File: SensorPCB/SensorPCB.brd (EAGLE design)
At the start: 37 x 65 mm, 31 parts, among them T1 33u

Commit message: add GND
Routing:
- net GND: track 25.0 -> 75.0 mm, vias 3 -> 6
- net SWCLK: track 31.8 -> 31.2 mm

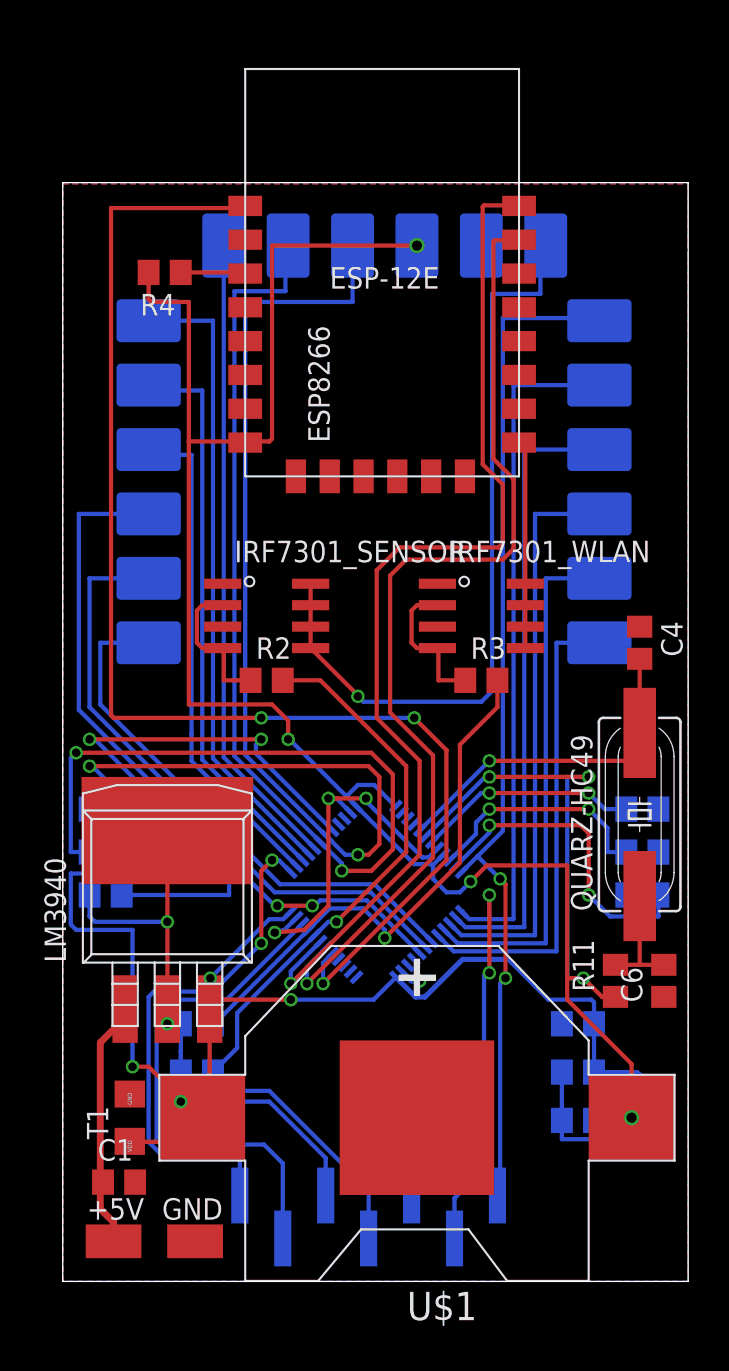
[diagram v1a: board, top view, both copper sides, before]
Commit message: edit tname and bname
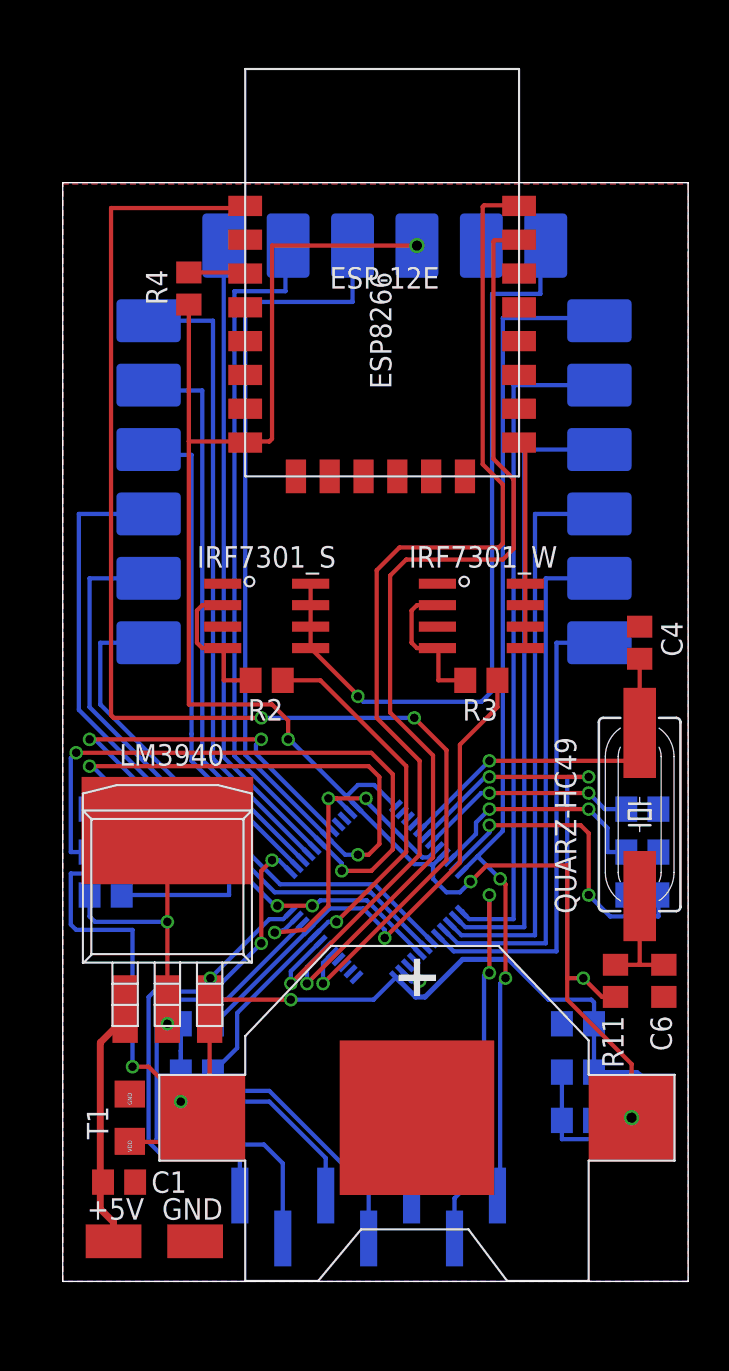
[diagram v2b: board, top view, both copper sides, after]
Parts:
- moved R4 1.72 mm to (7.46, 58.7), turned to 270 degrees
- renumbered IRF7301_SENSOR to IRF7301_S, IRF7301_WLAN to IRF7301_W
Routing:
- net +3V3: track 208.5 -> 204.3 mm

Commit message: closed #1
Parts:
- removed U$2: 5V_POWER_SUPPLY, 5V_POWER_SUPPLY:5V_POWER_SUPPLY
- added JP1: (no value), pinhead:1X02SMD
- moved C1 5.90 mm to (8.73, 3.49), turned to 270 degrees
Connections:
- net +5V: now also JP1.1; no longer U$2.MINUS
- net GND: now also JP1.2; no longer U$2.PLUS
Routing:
- net +5V: track 16.7 -> 19.3 mm
- net OSC_OUT: track 28.9 -> 27.9 mm
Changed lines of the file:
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@@
 <layers>
 <layer number="1" name="Top" color="4" fill="1" visible="yes" active="yes"/>
-<layer number="16" name="Bottom" color="1" fill="1" visible="no" active="yes"/>
+<layer number="16" name="Bottom" color="1" fill="1" visible="yes" active="yes"/>
 <layer number="17" name="Pads" color="2" fill="1" visible="yes" active="yes"/>
 <layer number="18" name="Vias" color="2" fill="1" visible="yes" active="yes"/>
@@
 <dimension x1="0" y1="0" x2="37" y2="0" x3="18.5" y3="-10" textsize="1.778" layer="1"/>
 <dimension x1="37" y1="0" x2="37" y2="65" x3="58.7375" y3="32.5" textsize="1.778" layer="1"/>
-<text x="1.42875" y="3.65125" size="1.27" layer="25">+5V</text>
-<text x="5.87375" y="3.65125" size="1.27" layer="25">GND</text>
+<text x="1.74625" y="0.79375" size="1.27" layer="25">+5V</text>
+<text x="4.445" y="5.3975" size="1.27" layer="25">GND</text>
 </plain>
 <attributes>
@@
 </autorouter>
 <elements>
-<element name="C1" library="rcl" package="C0805" value="470n" x="3.33375" y="5.87375" smashed="yes">
-<attribute name="NAME" x="5.23875" y="5.23875" size="1.27" layer="25"/>
-<attribute name="VALUE" x="2.06375" y="3.33375" size="1.27" layer="27"/>
+<element name="C1" library="rcl" package="C0805" value="470n" x="8.73125" y="3.4925" smashed="yes" rot="R270">
+<attribute name="NAME" x="8.09625" y="1.5875" size="1.27" layer="25" rot="R270"/>
+<attribute name="VALUE" x="6.19125" y="4.7625" size="1.27" layer="27" rot="R270"/>
 </element>
 <element name="C10" library="rcl" package="C0805" value="100n" x="34.29" y="27.94" smashed="yes" rot="MR180">
@@
 </element>
 <element name="U$5" library="breakout_base" package="BREAKOUT_FOOTPRINT_V1" value="BREAKOUT_FP_V1" x="33.655" y="63.1825" rot="MR270"/>
-<element name="U$2" library="5V_POWER_SUPPLY" package="5V_POWER_SUPPLY" value="5V_POWER_SUPPLY" x="5.3975" y="2.38125" rot="R180"/>
 <element name="R4" library="rcl" package="R0805" value="10k" x="7.46125" y="58.7375" smashed="yes" rot="R270">
 <attribute name="NAME" x="4.92125" y="59.84875" size="1.27" layer="25" rot="R270"/>
 <attribute name="VALUE" x="4.92125" y="59.3725" size="1.27" layer="27" rot="R270"/>
+</element>
+<element name="JP1" library="pinhead" package="1X02SMD" value="" x="5.08" y="3.65125" smashed="yes">
+<attribute name="VALUE" x="2.54" y="0.47625" size="1.27" layer="27"/>
 </element>
 </elements>
@@
 <contactref element="U$5" pad="P$17"/>
 <contactref element="U$1" pad="-"/>
-<contactref element="U$2" pad="PLUS"/>
 <polygon width="0.254" layer="1">
 <vertex x="0" y="64.92875"/>
@@
 <wire x1="6.9875" y1="15.24" x2="6.9875" y2="12.3825" width="0.254" layer="16"/>
 <wire x1="6.19125" y1="16.11" x2="6.19125" y2="15.39875" width="0.254" layer="1"/>
-<via x="6.19125" y="15.24" extent="1-16" drill="0.5"/>
-<wire x1="6.19125" y1="15.39875" x2="6.19125" y2="15.24" width="0.254" layer="1"/>
-<wire x1="6.19125" y1="15.24" x2="6.9875" y2="15.24" width="0.254" layer="16"/>
+<via x="6.35" y="15.24" extent="1-16" drill="0.5"/>
+<wire x1="6.19125" y1="15.39875" x2="6.35" y2="15.24" width="0.254" layer="1"/>
+<wire x1="6.35" y1="15.24" x2="6.9875" y2="15.24" width="0.254" layer="16"/>
 <wire x1="6.9875" y1="12.3825" x2="6.9875" y2="13.65" width="0.254" layer="16"/>
 <wire x1="6.9875" y1="13.65" x2="6.985" y2="13.6525" width="0.254" layer="16"/>
@@
 <wire x1="1.905" y1="21.2725" x2="6.19125" y2="21.2725" width="0.254" layer="16"/>
 <via x="6.19125" y="21.2725" extent="1-16" drill="0.5"/>
+<contactref element="JP1" pad="2"/>
 </signal>
 <signal name="+3V3">
@@
 <wire x1="7.62" y1="9.525" x2="6.9875" y2="9.525" width="0.254" layer="1"/>
 <wire x1="6.9875" y1="9.525" x2="6.985" y2="9.5275" width="0.254" layer="1"/>
-<wire x1="6.985" y1="9.5275" x2="6.985" y2="10.63625" width="0.254" layer="1"/>
+<wire x1="6.985" y1="9.5275" x2="6.985" y2="10.4775" width="0.254" layer="1"/>
 <wire x1="8.255" y1="9.68375" x2="8.69125" y2="10.12" width="0.254" layer="1"/>
 <wire x1="8.69125" y1="10.12" x2="8.69125" y2="16.11" width="0.254" layer="1"/>
@@
 <wire x1="4.1275" y1="12.7" x2="5.08" y2="12.7" width="0.254" layer="1"/>
 <wire x1="6.9875" y1="9.525" x2="6.985" y2="9.5275" width="0.254" layer="16"/>
-<wire x1="6.985" y1="9.5275" x2="6.985" y2="10.63625" width="0.254" layer="16"/>
-<via x="6.985" y="10.63625" extent="1-16" drill="0.5"/>
+<wire x1="6.985" y1="9.5275" x2="6.985" y2="10.4775" width="0.254" layer="16"/>
+<via x="6.985" y="10.4775" extent="1-16" drill="0.5"/>
 <wire x1="12.22375" y1="10.63625" x2="15.5575" y2="7.3025" width="0.254" layer="16"/>
-<wire x1="6.985" y1="10.63625" x2="12.22375" y2="10.63625" width="0.254" layer="16"/>
 <wire x1="5.08" y1="12.7" x2="6.985" y2="10.795" width="0.254" layer="1"/>
-<wire x1="6.985" y1="10.795" x2="6.985" y2="10.63625" width="0.254" layer="1"/>
+<wire x1="6.985" y1="10.795" x2="6.985" y2="10.4775" width="0.254" layer="1"/>
 <wire x1="7.46125" y1="57.7875" x2="7.46125" y2="49.68875" width="0.254" layer="1"/>
+<wire x1="6.985" y1="10.4775" x2="7.14375" y2="10.63625" width="0.254" layer="16"/>
+<wire x1="7.14375" y1="10.63625" x2="12.22375" y2="10.63625" width="0.254" layer="16"/>
 </signal>
 <signal name="+5V">
 <contactref element="LM3940" pad="1"/>
 <contactref element="C1" pad="1"/>
-<contactref element="U$2" pad="MINUS"/>
-<wire x1="3.0055" y1="3.18575" x2="3.0055" y2="2.37625" width="0.4064" layer="1"/>
-<wire x1="2.38375" y1="5.87375" x2="2.2225" y2="6.18875" width="0.4064" layer="1"/>
-<wire x1="2.2225" y1="6.18875" x2="2.2225" y2="4.28625" width="0.4064" layer="1"/>
-<wire x1="2.2225" y1="4.28625" x2="3.0055" y2="3.50325" width="0.4064" layer="1"/>
-<wire x1="3.0055" y1="3.50325" x2="3.0055" y2="2.37625" width="0.4064" layer="1"/>
-<wire x1="2.38375" y1="5.87375" x2="2.2225" y2="6.19375" width="0.4064" layer="1"/>
-<wire x1="2.2225" y1="6.19375" x2="2.2225" y2="14.12875" width="0.4064" layer="1"/>
+<wire x1="2.2225" y1="6.50875" x2="2.2225" y2="14.12875" width="0.4064" layer="1"/>
 <wire x1="4.1675" y1="16.07375" x2="3.69125" y2="16.11" width="0.4064" layer="1"/>
 <wire x1="2.2225" y1="14.12875" x2="3.69125" y2="15.5975" width="0.4064" layer="1"/>
 <wire x1="3.69125" y1="15.5975" x2="3.69125" y2="16.11" width="0.4064" layer="1"/>
+<contactref element="JP1" pad="1"/>
+<wire x1="3.81" y1="4.92125" x2="2.2225" y2="6.50875" width="0.4064" layer="1"/>
+<wire x1="3.81" y1="4.92125" x2="3.96875" y2="5.08" width="0.4064" layer="1"/>
+<wire x1="8.73125" y1="4.4425" x2="8.73125" y2="5.23875" width="0.4064" layer="1"/>
+<wire x1="8.73125" y1="5.23875" x2="8.41375" y2="5.55625" width="0.4064" layer="1"/>
+<wire x1="8.41375" y1="5.55625" x2="5.08" y2="5.55625" width="0.4064" layer="1"/>
+<wire x1="5.08" y1="5.55625" x2="4.445" y2="4.92125" width="0.4064" layer="1"/>
+<wire x1="4.445" y1="4.92125" x2="3.81" y2="4.92125" width="0.4064" layer="1"/>
 </signal>
 <signal name="SWCLK">
@@
 <wire x1="29.845" y1="29.845" x2="29.845" y2="17.93875" width="0.254" layer="16"/>
 <wire x1="30.7975" y1="17.93875" x2="29.845" y2="17.93875" width="0.254" layer="16"/>
-<wire x1="29.845" y1="17.93875" x2="30.7975" y2="17.93875" width="0.254" layer="1"/>
+<wire x1="29.845" y1="17.93875" x2="30.7975" y2="17.93875" width="0" layer="19" extent="1-16"/>
 <wire x1="30.7975" y1="17.93875" x2="31.90875" y2="16.8275" width="0.254" layer="1"/>
 <wire x1="31.90875" y1="16.8275" x2="32.385" y2="16.8275" width="0.254" layer="1"/>

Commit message: closed #3
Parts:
- moved C1 7.35 mm to (1.59, 5.24)
- moved JP1 1.44 mm to (6.51, 3.49)
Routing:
- net GND: track 74.9 -> 88.1 mm
- net +5V: track 19.3 -> 15.5 mm
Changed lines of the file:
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@@
 <layer number="24" name="bOrigins" color="15" fill="1" visible="yes" active="yes"/>
 <layer number="25" name="tNames" color="7" fill="1" visible="yes" active="yes"/>
-<layer number="26" name="bNames" color="7" fill="1" visible="no" active="yes"/>
-<layer number="27" name="tValues" color="7" fill="1" visible="no" active="yes"/>
-<layer number="28" name="bValues" color="7" fill="1" visible="no" active="yes"/>
+<layer number="26" name="bNames" color="7" fill="1" visible="yes" active="yes"/>
+<layer number="27" name="tValues" color="7" fill="1" visible="yes" active="yes"/>
+<layer number="28" name="bValues" color="7" fill="1" visible="yes" active="yes"/>
 <layer number="29" name="tStop" color="7" fill="3" visible="yes" active="yes"/>
 <layer number="30" name="bStop" color="7" fill="6" visible="yes" active="yes"/>
@@
 <dimension x1="0" y1="0" x2="37" y2="0" x3="18.5" y3="-10" textsize="1.778" layer="1"/>
 <dimension x1="37" y1="0" x2="37" y2="65" x3="58.7375" y3="32.5" textsize="1.778" layer="1"/>
-<text x="1.74625" y="0.79375" size="1.27" layer="25">+5V</text>
-<text x="4.445" y="5.3975" size="1.27" layer="25">GND</text>
+<text x="6.19125" y="1.905" size="1.27" layer="25" rot="R180">+5V</text>
+<text x="9.8425" y="6.35" size="1.27" layer="25" rot="R180">GND</text>
 </plain>
 <attributes>
@@
 </autorouter>
 <elements>
-<element name="C1" library="rcl" package="C0805" value="470n" x="8.73125" y="3.4925" smashed="yes" rot="R270">
-<attribute name="NAME" x="8.09625" y="1.5875" size="1.27" layer="25" rot="R270"/>
-<attribute name="VALUE" x="6.19125" y="4.7625" size="1.27" layer="27" rot="R270"/>
+<element name="C1" library="rcl" package="C0805" value="470n" x="1.5875" y="5.23875" smashed="yes" rot="R270">
+<attribute name="NAME" x="0.9525" y="3.33375" size="1.27" layer="25" rot="R270"/>
+<attribute name="VALUE" x="-0.9525" y="6.50875" size="1.27" layer="27" rot="R270"/>
 </element>
 <element name="C10" library="rcl" package="C0805" value="100n" x="34.29" y="27.94" smashed="yes" rot="MR180">
@@
 <attribute name="VALUE" x="4.92125" y="59.3725" size="1.27" layer="27" rot="R270"/>
 </element>
-<element name="JP1" library="pinhead" package="1X02SMD" value="" x="5.08" y="3.65125" smashed="yes">
-<attribute name="VALUE" x="2.54" y="0.47625" size="1.27" layer="27"/>
+<element name="JP1" library="pinhead" package="1X02SMD" value="" x="6.50875" y="3.4925" smashed="yes">
+<attribute name="VALUE" x="3.96875" y="0.3175" size="1.27" layer="27"/>
 </element>
 </elements>
@@
 <vertex x="0" y="0"/>
 </polygon>
-<wire x1="20.066796875" y1="18.343721875" x2="20.63051875" y2="17.78" width="0.3048" layer="16"/>
-<wire x1="20.63051875" y1="17.78" x2="21.11375" y2="17.78" width="0.3048" layer="16"/>
-<wire x1="21.11375" y1="17.78" x2="21.2725" y2="17.78" width="0.3048" layer="16"/>
-<via x="21.11375" y="17.78" extent="1-16" drill="0.5"/>
 <wire x1="12.54125" y1="20.6375" x2="14.2875" y2="20.79625" width="0.254" layer="1"/>
 <wire x1="14.2875" y1="20.79625" x2="15.71625" y2="22.225" width="0.254" layer="1"/>
@@
 <via x="6.19125" y="21.2725" extent="1-16" drill="0.5"/>
 <contactref element="JP1" pad="2"/>
+<wire x1="20.066796875" y1="18.343721875" x2="20.94801875" y2="17.4625" width="0.254" layer="16"/>
+<wire x1="20.94801875" y1="17.4625" x2="21.2725" y2="17.4625" width="0.254" layer="16"/>
+<wire x1="20.955" y1="9.68375" x2="20.955" y2="19.05" width="0.254" layer="1"/>
+<wire x1="20.955" y1="19.05" x2="22.5425" y2="19.05" width="0.254" layer="1"/>
+<via x="22.5425" y="19.05" extent="1-16" drill="0.5"/>
+<wire x1="21.2725" y1="17.4625" x2="22.5425" y2="18.7325" width="0.254" layer="16"/>
+<wire x1="22.5425" y1="18.7325" x2="22.5425" y2="19.05" width="0.254" layer="16"/>
 </signal>
 <signal name="+3V3">
@@
 <wire x1="3.4925" y1="25.08" x2="3.4925" y2="24.13" width="0.254" layer="16"/>
 <wire x1="3.4925" y1="24.13" x2="0.47625" y2="24.13" width="0.254" layer="16"/>
-<wire x1="19.71324375" y1="17.99016875" x2="20.8759125" y2="16.8275" width="0.3048" layer="16"/>
-<wire x1="20.8759125" y1="16.8275" x2="21.43125" y2="16.8275" width="0.3048" layer="16"/>
-<wire x1="21.43125" y1="16.8275" x2="23.65375" y2="19.05" width="0.3048" layer="16"/>
-<wire x1="23.65375" y1="19.05" x2="26.3525" y2="19.05" width="0.3048" layer="16"/>
 <wire x1="17.379790625" y1="28.101796875" x2="20.79625" y2="24.6853375" width="0.254" layer="16"/>
 <wire x1="21.874553125" y1="24.60625" x2="21.795465625" y2="24.6853375" width="0.254" layer="16"/>
@@
 <wire x1="6.985" y1="10.4775" x2="7.14375" y2="10.63625" width="0.254" layer="16"/>
 <wire x1="7.14375" y1="10.63625" x2="12.22375" y2="10.63625" width="0.254" layer="16"/>
+<wire x1="19.71324375" y1="17.99016875" x2="20.7171625" y2="16.98625" width="0.254" layer="16"/>
+<wire x1="20.7171625" y1="16.98625" x2="21.43125" y2="16.98625" width="0.254" layer="16"/>
+<wire x1="21.43125" y1="16.98625" x2="23.495" y2="19.05" width="0.254" layer="16"/>
+<wire x1="23.495" y1="19.05" x2="26.3525" y2="19.05" width="0.254" layer="16"/>
 </signal>
 <signal name="+5V">
 <contactref element="LM3940" pad="1"/>
 <contactref element="C1" pad="1"/>
-<wire x1="2.2225" y1="6.50875" x2="2.2225" y2="14.12875" width="0.4064" layer="1"/>
 <wire x1="4.1675" y1="16.07375" x2="3.69125" y2="16.11" width="0.4064" layer="1"/>
-<wire x1="2.2225" y1="14.12875" x2="3.69125" y2="15.5975" width="0.4064" layer="1"/>
+<wire x1="1.5875" y1="13.49375" x2="3.69125" y2="15.5975" width="0.4064" layer="1"/>
 <wire x1="3.69125" y1="15.5975" x2="3.69125" y2="16.11" width="0.4064" layer="1"/>
 <contactref element="JP1" pad="1"/>
-<wire x1="3.81" y1="4.92125" x2="2.2225" y2="6.50875" width="0.4064" layer="1"/>
-<wire x1="3.81" y1="4.92125" x2="3.96875" y2="5.08" width="0.4064" layer="1"/>
-<wire x1="8.73125" y1="4.4425" x2="8.73125" y2="5.23875" width="0.4064" layer="1"/>
-<wire x1="8.73125" y1="5.23875" x2="8.41375" y2="5.55625" width="0.4064" layer="1"/>
-<wire x1="8.41375" y1="5.55625" x2="5.08" y2="5.55625" width="0.4064" layer="1"/>
-<wire x1="5.08" y1="5.55625" x2="4.445" y2="4.92125" width="0.4064" layer="1"/>
-<wire x1="4.445" y1="4.92125" x2="3.81" y2="4.92125" width="0.4064" layer="1"/>
+<wire x1="1.5875" y1="13.49375" x2="1.5875" y2="6.18875" width="0.4064" layer="1"/>
+<wire x1="1.5875" y1="6.18875" x2="1.59" y2="6.19125" width="0.4064" layer="1"/>
+<wire x1="1.59" y1="6.19125" x2="3.65125" y2="6.19125" width="0.4064" layer="1"/>
+<wire x1="3.65125" y1="6.19125" x2="5.08" y2="4.7625" width="0.4064" layer="1"/>
+<wire x1="5.08" y1="4.7625" x2="5.23875" y2="4.7625" width="0.4064" layer="1"/>
 </signal>
 <signal name="SWCLK">
@@
 <wire x1="29.845" y1="29.845" x2="29.845" y2="17.93875" width="0.254" layer="16"/>
 <wire x1="30.7975" y1="17.93875" x2="29.845" y2="17.93875" width="0.254" layer="16"/>
-<wire x1="29.845" y1="17.93875" x2="30.7975" y2="17.93875" width="0" layer="19" extent="1-16"/>
 <wire x1="30.7975" y1="17.93875" x2="31.90875" y2="16.8275" width="0.254" layer="1"/>
 <wire x1="31.90875" y1="16.8275" x2="32.385" y2="16.8275" width="0.254" layer="1"/>
